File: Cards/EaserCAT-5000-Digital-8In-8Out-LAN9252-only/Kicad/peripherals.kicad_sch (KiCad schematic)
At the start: 41 parts, among them J1 24V Field, J10 24V_Common, J2 In5-8, J3 In1-4, J4 Output3-4, J5 Output7-8, J6 Output1-2, J7 Output5-6, J9 24V_common_selector, U1 TLP292-4, U2 TLP292-4, U4 TLP292-4, U5 TLP292-4

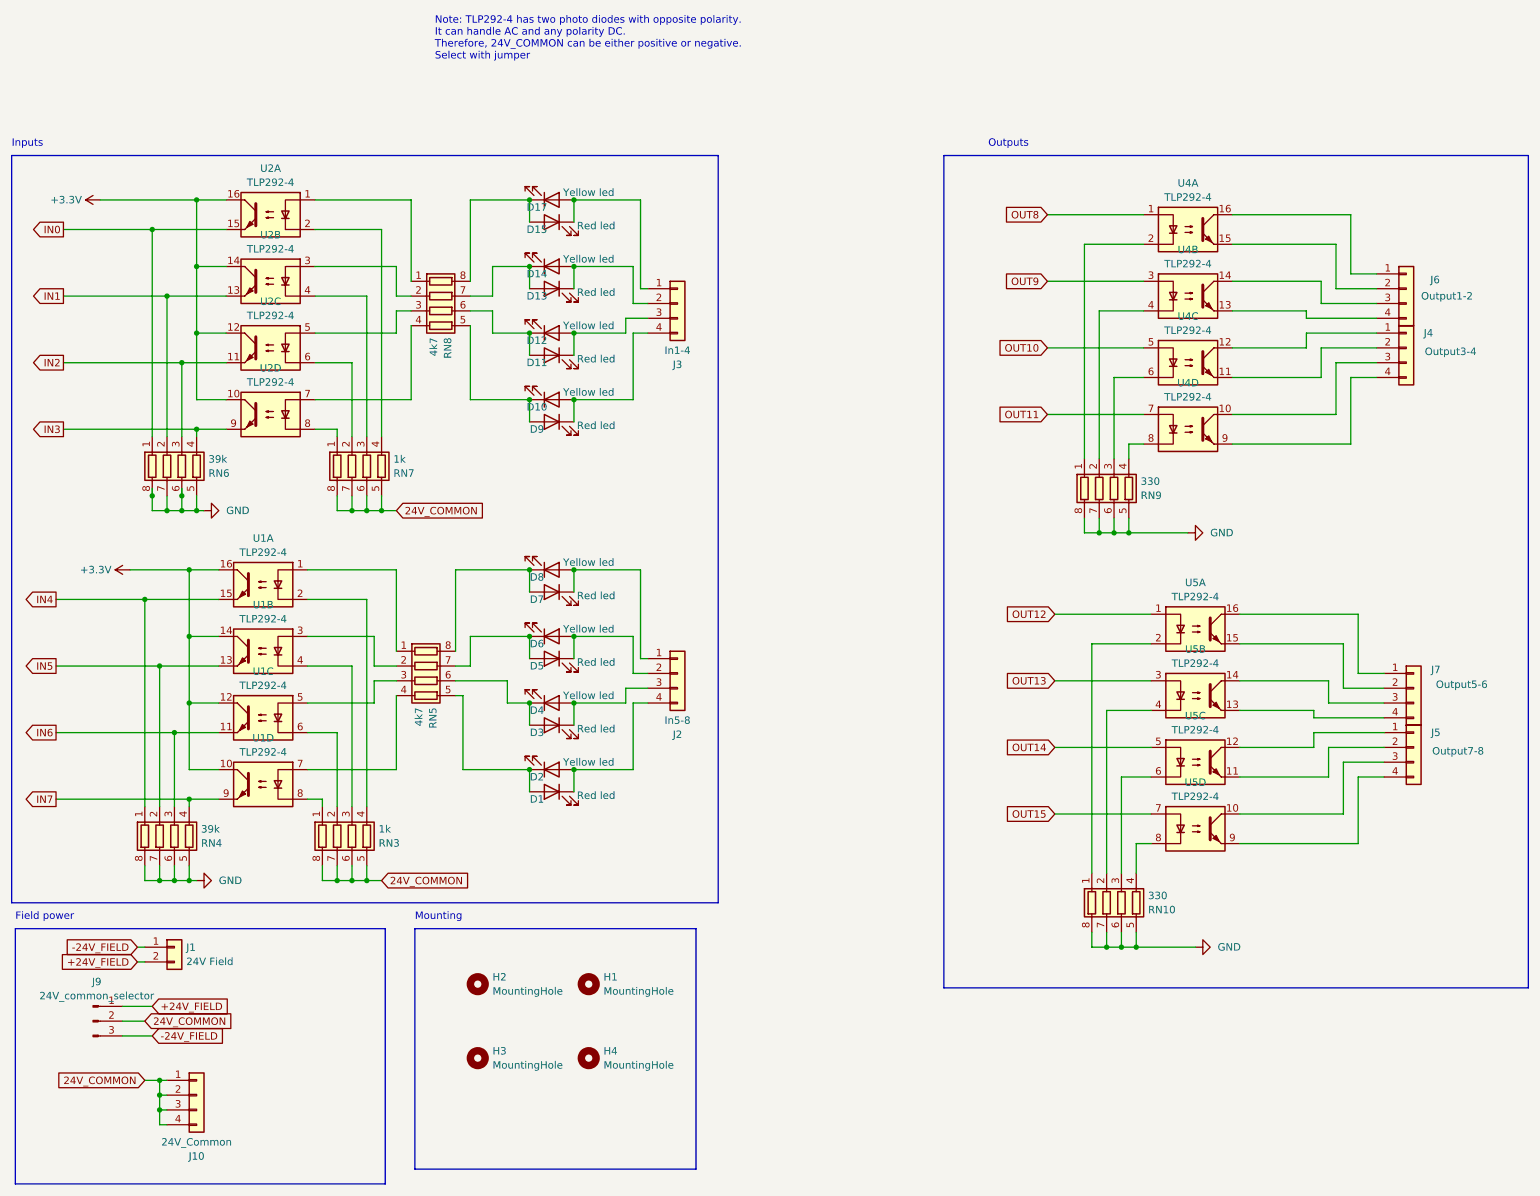
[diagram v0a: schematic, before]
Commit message: Updated 24V field voltage routing. Files sent for fab
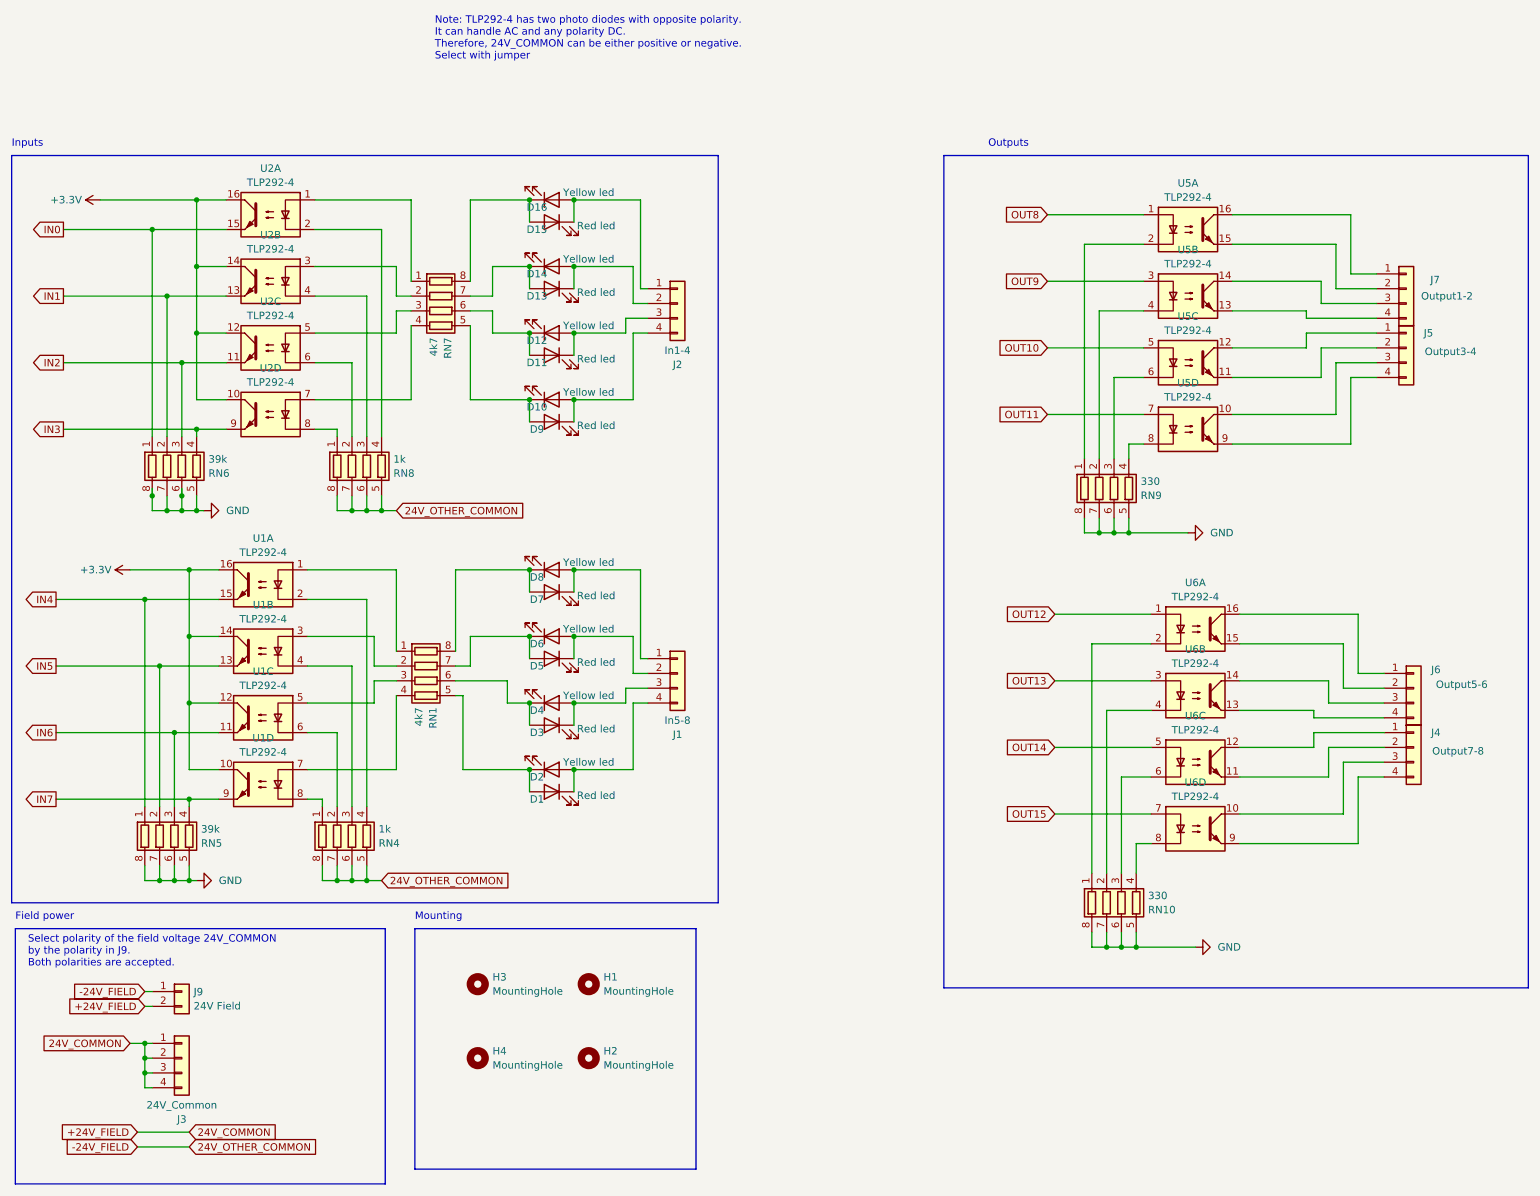
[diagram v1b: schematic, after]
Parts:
- removed J9: 24V_common_selector, Connector_PinHeader_2.54mm:PinHeader_1x03_P2.54mm_Vertical, symbol Connector:Conn_01x03_Pin
- renumbered D17 to D16, H4 to H2, H2 to H3, H3 to H4, J2 to J1, J3 to J2, J10 to J3, J5 to J4, J4 to J5, J7 to J6, J6 to J7, J1 to J9, RN5 to RN1, RN3 to RN4, RN4 to RN5, RN8 to RN7, RN7 to RN8, U4 to U5, U5 to U6
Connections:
- net +24V_FIELD: now also J3.1 (Pin_1), J3.2 (Pin_2), J3.3 (Pin_3), J3.4 (Pin_4)
- net -24V_FIELD: now also RN4.5 (R4.2), RN4.6 (R3.2), RN4.7 (R2.2), RN4.8 (R1.2), RN8.5 (R4.2), RN8.6 (R3.2), RN8.7 (R2.2), RN8.8 (R1.2)
- removed net 24V_COMMON: J3.1 (Pin_1), J3.2 (Pin_2), J3.3 (Pin_3), J3.4 (Pin_4), RN4.5 (R4.2), RN4.6 (R3.2), RN4.7 (R2.2), RN4.8 (R1.2), RN8.5 (R4.2), RN8.6 (R3.2), RN8.7 (R2.2), RN8.8 (R1.2)
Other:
- note added: "Select polarity of the field voltage 24V_COMMON by the polarity in J9. Both polarities are accepted."
- moved on the sheet: J3, J9
